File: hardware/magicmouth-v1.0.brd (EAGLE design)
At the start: 100 x 80 mm, 109 parts, among them IC1 LM386N, IC2 ATMEGA328P_PDIP, Q1 16Mhz, U1 ARDUINOR3-NOIOREF-NOTEXT

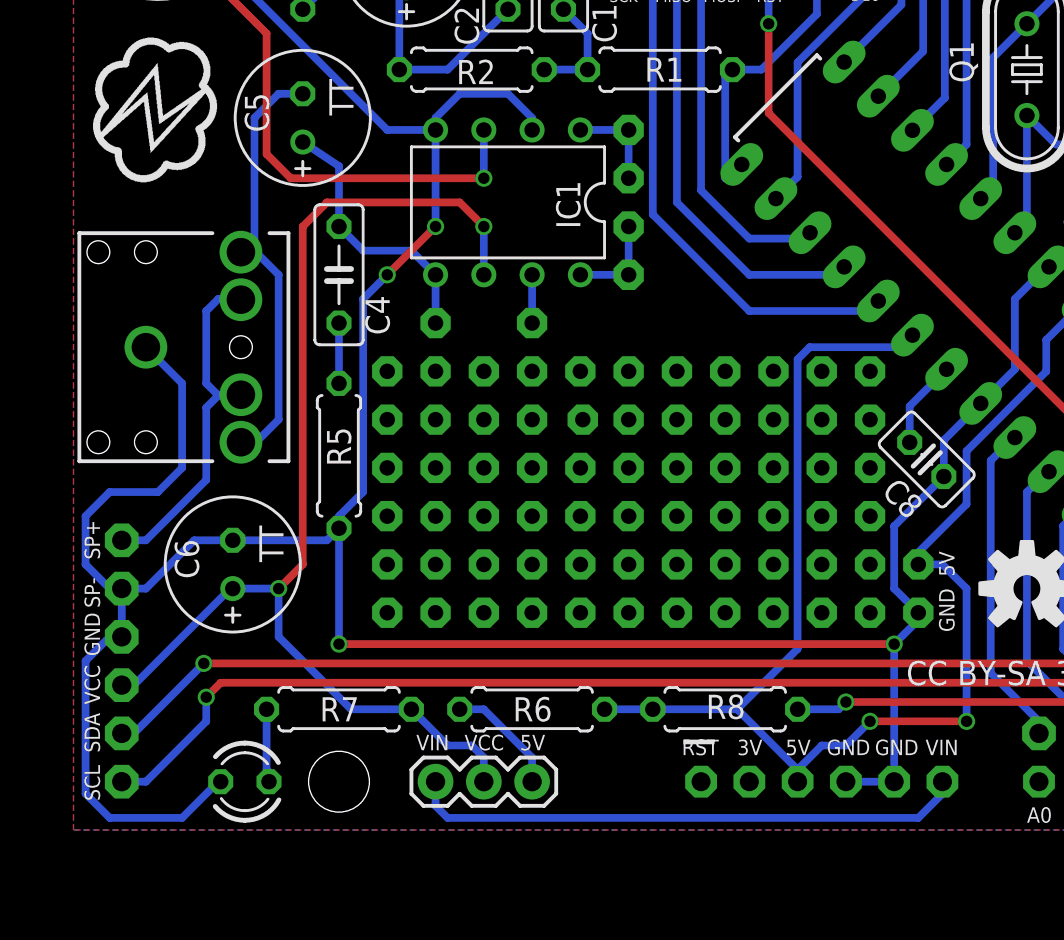
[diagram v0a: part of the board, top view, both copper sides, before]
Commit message: v0.1 and v1.0 eagle files
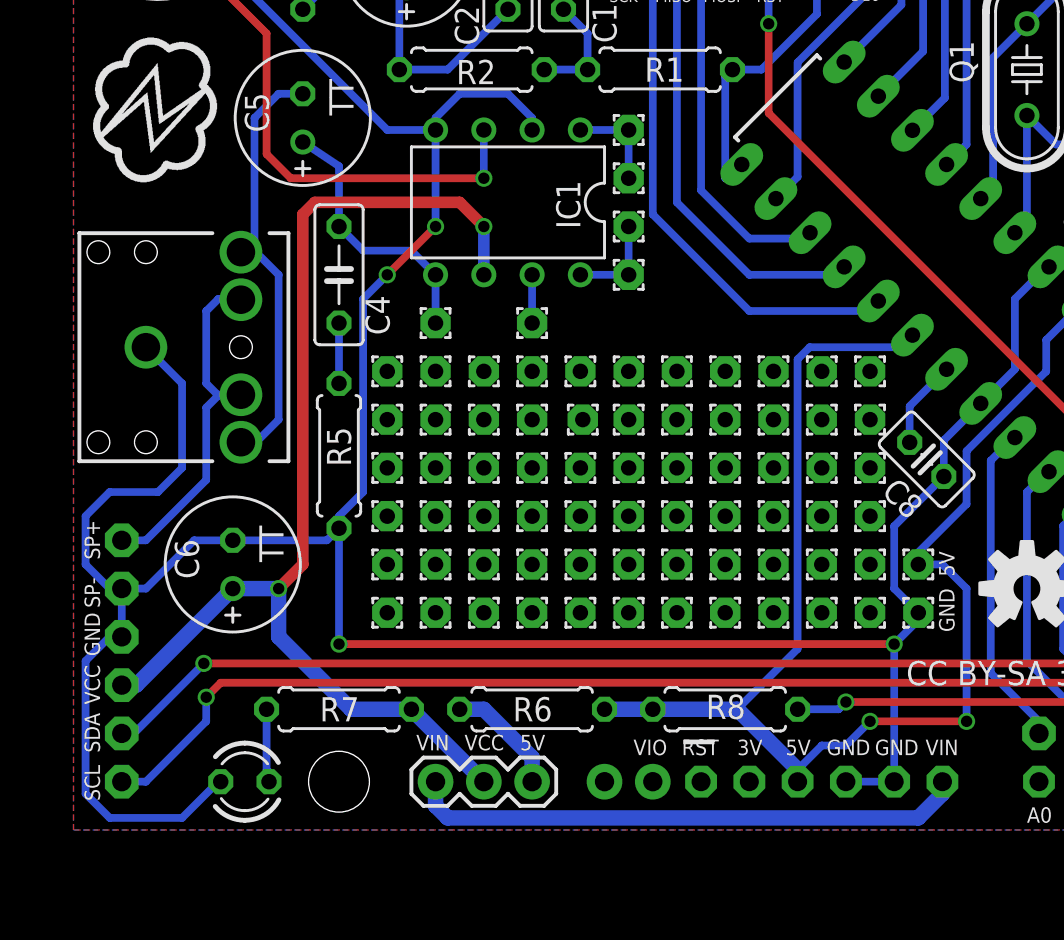
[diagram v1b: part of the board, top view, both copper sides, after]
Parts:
- added JP12: (no value), SparkFun:1X02_NO_SILK
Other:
- board text added: "VIO"
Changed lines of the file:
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@@
 <rectangle x1="10.8966" y1="47.1932" x2="11.557" y2="47.2186" layer="21" rot="R90"/>
 <rectangle x1="11.0109" y1="47.1805" x2="11.3919" y2="47.2059" layer="21" rot="R90"/>
+<text x="39.624" y="14.097" size="0.8128" layer="21" font="vector">VIO</text>
 </plain>
 <attributes>
@@
 </element>
 <element name="U$1" library="SparkFun" package="OSHW-LOGO-M" value="" x="60.325" y="22.86"/>
+<element name="JP12" library="SparkFun" package="1X02_NO_SILK" value="" x="38.1" y="12.7" smashed="yes">
+<attribute name="VALUE" x="36.83" y="9.525" size="1.27" layer="27"/>
+</element>
 </elements>
 <signals>
@@
 <contactref element="C6" pad="+"/>
 <contactref element="R7" pad="2"/>
-<wire x1="27.94" y1="16.51" x2="29.845" y2="14.605" width="0.4064" layer="16"/>
-<wire x1="29.845" y1="14.605" x2="31.115" y2="14.605" width="0.4064" layer="16"/>
-<wire x1="31.115" y1="14.605" x2="31.75" y2="13.97" width="0.4064" layer="16"/>
-<wire x1="31.75" y1="39.37" x2="31.75" y2="41.91" width="0.4064" layer="16"/>
-<wire x1="31.75" y1="41.91" x2="30.48" y2="43.18" width="0.4064" layer="1"/>
-<wire x1="30.48" y1="43.18" x2="23.495" y2="43.18" width="0.4064" layer="1"/>
-<wire x1="23.495" y1="43.18" x2="22.225" y2="41.91" width="0.4064" layer="1"/>
-<wire x1="22.225" y1="41.91" x2="22.225" y2="24.13" width="0.4064" layer="1"/>
-<wire x1="22.225" y1="24.13" x2="20.955" y2="22.86" width="0.4064" layer="1"/>
 <via x="20.955" y="22.86" extent="1-16" drill="0.6" shape="square"/>
 <via x="31.75" y="41.91" extent="1-16" drill="0.6" shape="square"/>
 <contactref element="JP1" pad="2"/>
-<wire x1="31.75" y1="12.7" x2="31.75" y2="13.97" width="0.4064" layer="16"/>
 <contactref element="JP3" pad="4"/>
-<wire x1="27.94" y1="16.51" x2="24.765" y2="16.51" width="0.4064" layer="16"/>
-<wire x1="12.7" y1="17.78" x2="13.335" y2="17.78" width="0.4064" layer="16"/>
-<wire x1="20.955" y1="22.86" x2="18.542" y2="22.86" width="0.4064" layer="16"/>
-<wire x1="18.542" y1="22.86" x2="18.415" y2="22.86" width="0.4064" layer="16"/>
-<wire x1="18.415" y1="22.86" x2="13.335" y2="17.78" width="0.4064" layer="16"/>
-<wire x1="20.955" y1="22.86" x2="20.955" y2="20.32" width="0.4064" layer="16"/>
-<wire x1="20.955" y1="20.32" x2="24.765" y2="16.51" width="0.4064" layer="16"/>
+<wire x1="12.7" y1="17.78" x2="13.462" y2="17.78" width="0.8128" layer="16"/>
+<wire x1="13.462" y1="17.78" x2="18.542" y2="22.86" width="0.8128" layer="16"/>
+<wire x1="18.542" y1="22.86" x2="20.955" y2="22.86" width="0.8128" layer="16"/>
+<wire x1="31.75" y1="12.7" x2="27.94" y2="16.51" width="0.8128" layer="16"/>
+<wire x1="27.94" y1="16.51" x2="24.765" y2="16.51" width="0.8128" layer="16"/>
+<wire x1="24.765" y1="16.51" x2="20.955" y2="20.32" width="0.8128" layer="16"/>
+<wire x1="20.955" y1="20.32" x2="20.955" y2="22.86" width="0.8128" layer="16"/>
+<wire x1="20.955" y1="22.86" x2="22.225" y2="24.13" width="0.6096" layer="1"/>
+<wire x1="22.225" y1="24.13" x2="22.225" y2="42.545" width="0.6096" layer="1"/>
+<wire x1="22.225" y1="42.545" x2="22.86" y2="43.18" width="0.6096" layer="1"/>
+<wire x1="22.86" y1="43.18" x2="30.48" y2="43.18" width="0.6096" layer="1"/>
+<wire x1="30.48" y1="43.18" x2="31.75" y2="41.91" width="0.6096" layer="1"/>
+<wire x1="31.75" y1="41.91" x2="31.75" y2="39.37" width="0.6096" layer="16"/>
 </signal>
 <signal name="N$7">
 <contactref element="R6" pad="1"/>
-<wire x1="34.29" y1="13.97" x2="31.75" y2="16.51" width="0.4064" layer="16"/>
-<wire x1="31.75" y1="16.51" x2="30.48" y2="16.51" width="0.4064" layer="16"/>
 <contactref element="JP1" pad="1"/>
-<wire x1="34.29" y1="12.7" x2="34.29" y2="13.97" width="0.4064" layer="16"/>
+<wire x1="30.48" y1="16.51" x2="31.75" y2="16.51" width="0.8128" layer="16"/>
+<wire x1="31.75" y1="16.51" x2="34.29" y2="13.97" width="0.8128" layer="16"/>
+<wire x1="34.29" y1="13.97" x2="34.29" y2="12.7" width="0.8128" layer="16"/>
 </signal>
 <signal name="N$10">
@@
 <signal name="VIN">
 <contactref element="U1" pad="VIN"/>
-<wire x1="55.88" y1="12.7" x2="55.88" y2="12.065" width="0.4064" layer="16"/>
-<wire x1="55.88" y1="12.065" x2="54.61" y2="10.795" width="0.4064" layer="16"/>
-<wire x1="54.61" y1="10.795" x2="29.845" y2="10.795" width="0.4064" layer="16"/>
-<wire x1="29.845" y1="10.795" x2="29.21" y2="11.43" width="0.4064" layer="16"/>
 <contactref element="JP1" pad="3"/>
-<wire x1="29.21" y1="11.43" x2="29.21" y2="12.7" width="0.4064" layer="16"/>
+<wire x1="55.88" y1="12.7" x2="55.88" y2="12.065" width="0.8128" layer="16"/>
+<wire x1="55.88" y1="12.065" x2="54.61" y2="10.795" width="0.8128" layer="16"/>
+<wire x1="54.61" y1="10.795" x2="29.845" y2="10.795" width="0.8128" layer="16"/>
+<wire x1="29.845" y1="10.795" x2="29.21" y2="11.43" width="0.8128" layer="16"/>
+<wire x1="29.21" y1="11.43" x2="29.21" y2="12.7" width="0.8128" layer="16"/>
 </signal>
 <signal name="N$13">
@@
 <wire x1="65.731525" y1="40.440471875" x2="65.731525" y2="40.331525" width="0.4064" layer="16"/>
 <wire x1="61.341" y1="35.941" x2="65.731525" y2="40.331525" width="0.4064" layer="16"/>
-<wire x1="40.64" y1="16.51" x2="45.085" y2="16.51" width="0.4064" layer="16"/>
-<wire x1="40.64" y1="16.51" x2="38.1" y2="16.51" width="0.4064" layer="16"/>
-<wire x1="45.085" y1="16.51" x2="48.26" y2="13.335" width="0.4064" layer="16"/>
-<wire x1="48.26" y1="13.335" x2="48.26" y2="12.7" width="0.4064" layer="16"/>
 <wire x1="57.15" y1="15.875" x2="57.15" y2="22.86" width="0.4064" layer="16"/>
 <wire x1="48.26" y1="34.925" x2="48.26" y2="19.685" width="0.4064" layer="16"/>
@@
 <wire x1="57.15" y1="22.86" x2="55.88" y2="24.13" width="0.4064" layer="16"/>
 <wire x1="61.341" y1="35.941" x2="63.2821" y2="37.99105" width="0" layer="19" extent="16-16"/>
+<wire x1="48.26" y1="12.7" x2="48.26" y2="13.335" width="0.8128" layer="16"/>
+<wire x1="48.26" y1="13.335" x2="45.085" y2="16.51" width="0.8128" layer="16"/>
+<wire x1="45.085" y1="16.51" x2="40.64" y2="16.51" width="0.8128" layer="16"/>
+<wire x1="40.64" y1="16.51" x2="38.1" y2="16.51" width="0.8128" layer="16"/>
 </signal>
 <signal name="MOSI">
